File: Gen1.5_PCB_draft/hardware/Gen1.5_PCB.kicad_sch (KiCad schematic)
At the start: 45 parts, among them IC1 TJA1050T, J10 jumper2, J12 Enc2, J13 Enc3, J14 Enc4, J15 Enc5, J16 Enc6, J2 Booster, J3 Enc1, J4 jumper1, J5 Roboclaw1, J6 Roboclaw2, J7 Roboclaw3, U1 ESP32-P4-ETH, U2 4754, U8 level shifter

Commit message: fixed pcb
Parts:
- removed J10: jumper2, Gen1.5_PCB:CONN_3pin_jumper, symbol Connector_Generic:Conn_01x03
- removed J4: jumper1, Gen1.5_PCB:CONN_3pin_jumper, symbol Connector_Generic:Conn_01x03
- added S5: jumper1, Gen1.5_PCB:switch, symbol Gen1.5_PCB:switch
- added S6: jumper2, Gen1.5_PCB:switch, symbol Gen1.5_PCB:switch
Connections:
- net CANH: now also S5.3
- net CANL: now also S6.3
- net RX1: now also S5.1
- net TX1: now also S6.1
- net at J5.2 (Pin_2): now also S6.2
- net at J5.3 (Pin_3): now also S5.2

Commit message: added test points
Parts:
- added TP5, TP6, TP7: 5003, Gen1.5_PCB:test_point, symbol Gen1.5_PCB:5003
- J12: value Enc2 -> Enc3
- J13: value Enc3 -> Enc1
- J14: value Enc4 -> Enc6
- J15: value Enc5 -> Enc4
- J16: value Enc6 -> Enc2
- J3: value Enc1 -> Enc5
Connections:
- net 10V: now also TP7.TP
- net 3V3: now also TP5.TP
- net 5V: now also TP6.TP

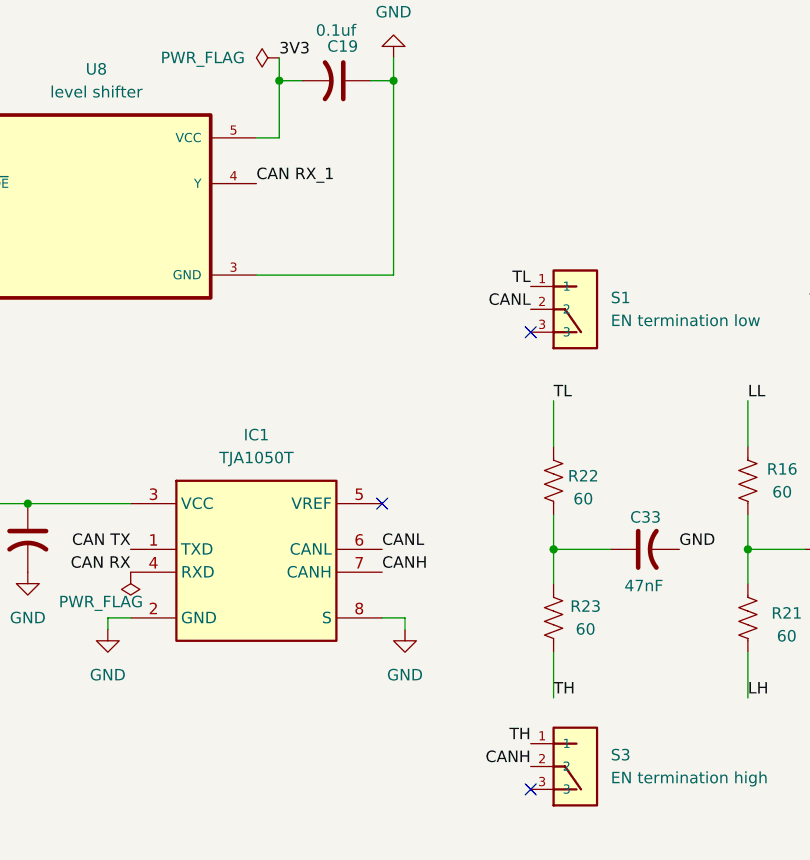
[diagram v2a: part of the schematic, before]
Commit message: added can test points
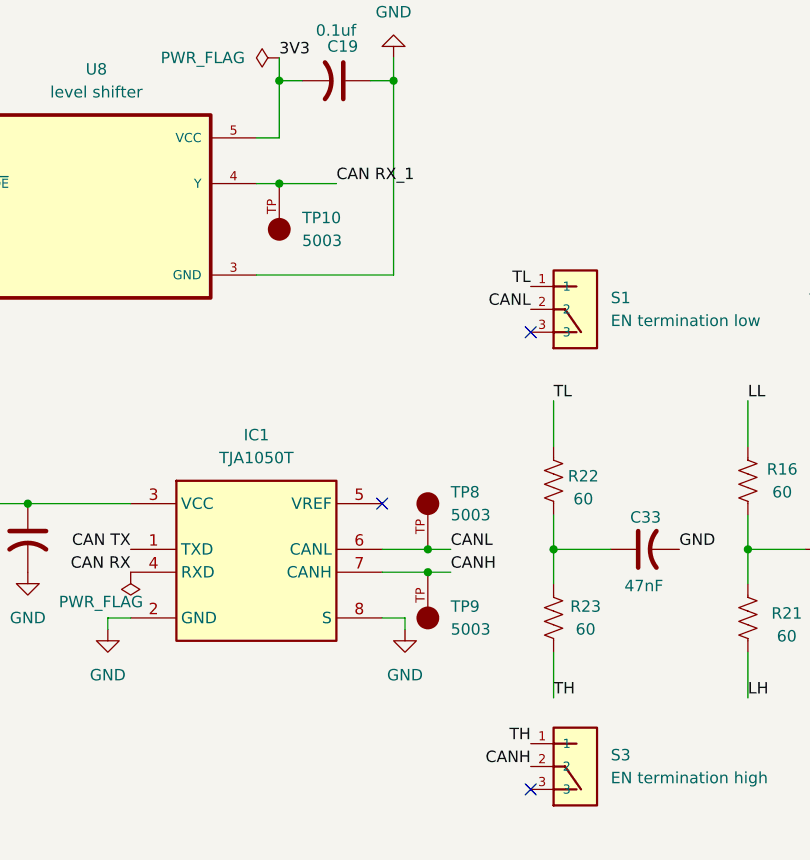
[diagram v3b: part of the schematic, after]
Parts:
- added TP10, TP8, TP9: 5003, Gen1.5_PCB:test_point, symbol Gen1.5_PCB:5003
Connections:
- net CAN RX_1: now also TP10.TP
- net CANH: now also TP9.TP
- net CANL: now also TP8.TP

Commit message: final changes before DR
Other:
- note added: "CAN"
- moved on the sheet: J2, TP7
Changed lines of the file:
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@@
 	)
 	(rectangle
-		(start 95.25 39.37)
-		(end 119.38 57.15)
+		(start 92.71 27.94)
+		(end 128.27 50.8)
 		(stroke
 			(width 0.381)
@@
 	(rectangle
 		(start 115.57 140.97)
-		(end 162.56 195.58)
+		(end 165.1 195.58)
 		(stroke
 			(width 0.381)
@@
 		)
 	)
+	(rectangle
+		(start 138.43 15.24)
+		(end 284.48 109.22)
+		(stroke
+			(width 0.381)
+			(type solid)
+			(color 0 255 0 1)
+		)
+		(fill
+			(type none)
+		)
+	)
 	(text "Boost conv"
 		(exclude_from_sim no)
-		(at 106.934 41.91 0)
+		(at 110.744 30.48 0)
 		(effects
 			(font
@@
 	(text ""
 		(exclude_from_sim no)
-		(at 96.52 54.356 0)
+		(at 100.33 42.926 0)
 		(effects
 			(font
@@
 		)
 	)
+	(text "CAN"
+		(exclude_from_sim no)
+		(at 225.044 19.558 0)
+		(effects
+			(font
+				(size 3.81 3.81)
+				(thickness 0.762)
+				(bold yes)
+				(color 0 255 0 1)
+			)
+		)
+	)
 	(text "load cells"
 		(exclude_from_sim no)
@@
 	(text ""
 		(exclude_from_sim no)
-		(at 120.65 55.626 0)
+		(at 124.46 44.196 0)
 		(effects
 			(font
@@
 	)
 	(junction
-		(at 102.87 53.34)
+		(at 106.68 41.91)
 		(diameter 0)
 		(color 0 0 0 0)
@@
 	)
 	(no_connect
-		(at 102.87 45.72)
+		(at 106.68 34.29)
 	)
 	(no_connect
@@
 	(wire
 		(pts
-			(xy 102.87 54.61) (xy 102.87 53.34)
+			(xy 106.68 43.18) (xy 106.68 41.91)
 		)
 		(stroke
@@
 	)
 	(label "GND"
-		(at 102.87 48.26 180)
+		(at 106.68 36.83 180)
 		(effects
 			(font
@@
 	)
 	(label "5V"
-		(at 102.87 50.8 180)
+		(at 106.68 39.37 180)
 		(effects
 			(font
@@
 	(global_label "10V"
 		(shape input)
-		(at 102.87 54.61 180)
+		(at 106.68 43.18 180)
 		(fields_autoplaced yes)
 		(effects
@@
 		)
 		(property "Intersheetrefs" "${INTERSHEET_REFS}"
-			(at 96.3772 54.61 0)
+			(at 100.1872 43.18 0)
 			(hide yes)
 			(show_name no)
@@
 	(symbol
 		(lib_id "Connector_Generic:Conn_01x04")
-		(at 107.95 48.26 0)
+		(at 111.76 36.83 0)
 		(unit 1)
 		(body_style 1)
@@
 		(fields_autoplaced yes)
 		(property "Reference" "J2"
-			(at 110.49 48.2599 0)
+			(at 114.3 36.8299 0)
 			(show_name no)
 			(do_not_autoplace no)
@@
 		)
 		(property "Value" "Booster"
-			(at 110.49 50.7999 0)
+			(at 114.3 39.3699 0)
 			(show_name no)
 			(do_not_autoplace no)
@@
 		)
 		(property "Footprint" "Gen1.5_PCB:booster headers"
-			(at 107.95 48.26 0)
+			(at 111.76 36.83 0)
 			(hide yes)
 			(show_name no)
@@
 		)
 		(property "Datasheet" ""
-			(at 107.95 48.26 0)
+			(at 111.76 36.83 0)
 			(hide yes)
 			(show_name no)
@@
 		)
 		(property "Description" "Generic connector, single row, 01x04, script generated (kicad-library-utils/schlib/autogen/connector/)"
-			(at 107.95 48.26 0)
+			(at 111.76 36.83 0)
 			(hide yes)
 			(show_name no)
@@
 		)
 		(property "LCSC" ""
-			(at 107.95 48.26 0)
+			(at 111.76 36.83 0)
 			(hide yes)
 			(show_name no)
@@
 	(symbol
 		(lib_id "Gen1.5_PCB:5003")
-		(at 102.87 58.42 270)
+		(at 106.68 46.99 270)
 		(unit 1)
 		(body_style 1)
@@
 		(fields_autoplaced yes)
 		(property "Reference" "TP7"
-			(at 105.41 57.1499 90)
+			(at 109.22 45.7199 90)
 			(show_name no)
 			(do_not_autoplace no)
@@
 		)
 		(property "Value" "5003"
-			(at 105.41 59.6899 90)
+			(at 109.22 48.2599 90)
 			(show_name no)
 			(do_not_autoplace no)
@@
 		)
 		(property "Footprint" "Gen1.5_PCB:test_point"
-			(at 102.87 58.42 0)
+			(at 106.68 46.99 0)
 			(hide yes)
 			(show_name no)
@@
 		)
 		(property "Datasheet" ""
-			(at 102.87 58.42 0)
+			(at 106.68 46.99 0)
 			(hide yes)
 			(show_name no)
@@
 		)
 		(property "Description" ""
-			(at 102.87 58.42 0)
+			(at 106.68 46.99 0)
 			(hide yes)
 			(show_name no)
@@
 		)
 		(property "PARTREV" "H"
-			(at 102.87 58.42 0)
+			(at 106.68 46.99 0)
 			(hide yes)
 			(show_name no)
@@
 		)
 		(property "STANDARD" "Manufacturer Recommendations"
-			(at 102.87 58.42 0)
+			(at 106.68 46.99 0)
 			(hide yes)
 			(show_name no)
@@
 		)
 		(property "SNAPEDA_PN" "5000"
-			(at 102.87 58.42 0)
+			(at 106.68 46.99 0)
 			(hide yes)
 			(show_name no)
@@
 		)
 		(property "MAXIMUM_PACKAGE_HEIGHT" "4.57 mm"
-			(at 102.87 58.42 0)
+			(at 106.68 46.99 0)
 			(hide yes)
 			(show_name no)
@@
 		)
 		(property "MANUFACTURER" "Keystone"
-			(at 102.87 58.42 0)
+			(at 106.68 46.99 0)
 			(hide yes)
 			(show_name no)
@@
 		)
 		(property "LCSC" "C238124"
-			(at 102.87 58.42 90)
+			(at 106.68 46.99 90)
 			(hide yes)
 			(show_name no)
@@
 	(symbol
 		(lib_id "power:PWR_FLAG")
-		(at 102.87 50.8 90)
+		(at 106.68 39.37 90)
 		(unit 1)
 		(body_style 1)
@@
 		(fields_autoplaced yes)
 		(property "Reference" "#FLG02"
-			(at 100.965 50.8 0)
+			(at 104.775 39.37 0)
 			(hide yes)
 			(show_name no)
@@
 		)
 		(property "Value" "PWR_FLAG"
-			(at 99.06 50.7999 90)
+			(at 102.87 39.3699 90)
 			(show_name no)
 			(do_not_autoplace no)
@@
 		)
 		(property "Footprint" ""
-			(at 102.87 50.8 0)
+			(at 106.68 39.37 0)
 			(hide yes)
 			(show_name no)
@@
 		)
 		(property "Datasheet" ""
-			(at 102.87 50.8 0)
+			(at 106.68 39.37 0)
 			(hide yes)
 			(show_name no)
@@
 		)
 		(property "Description" "Special symbol for telling ERC where power comes from"
-			(at 102.87 50.8 0)
+			(at 106.68 39.37 0)
 			(hide yes)
 			(show_name no)

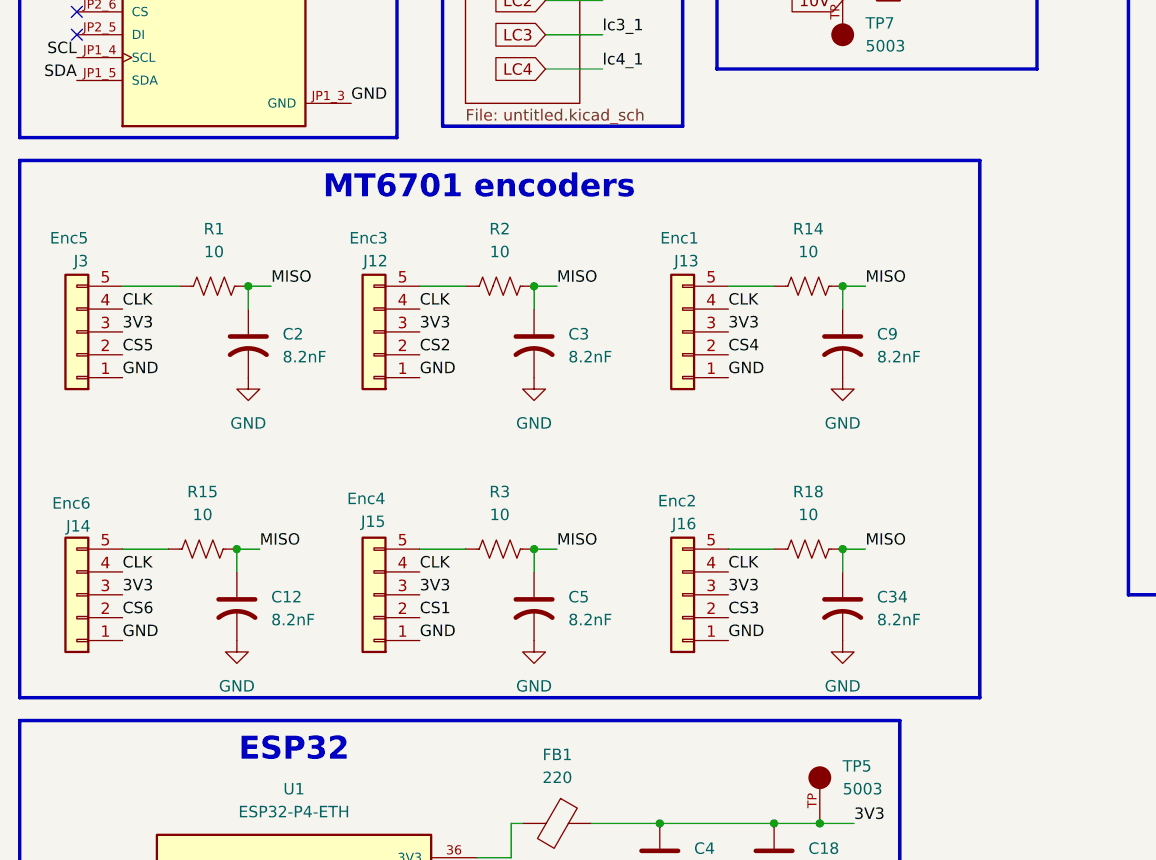
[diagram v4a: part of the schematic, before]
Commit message: finished mcp connector design
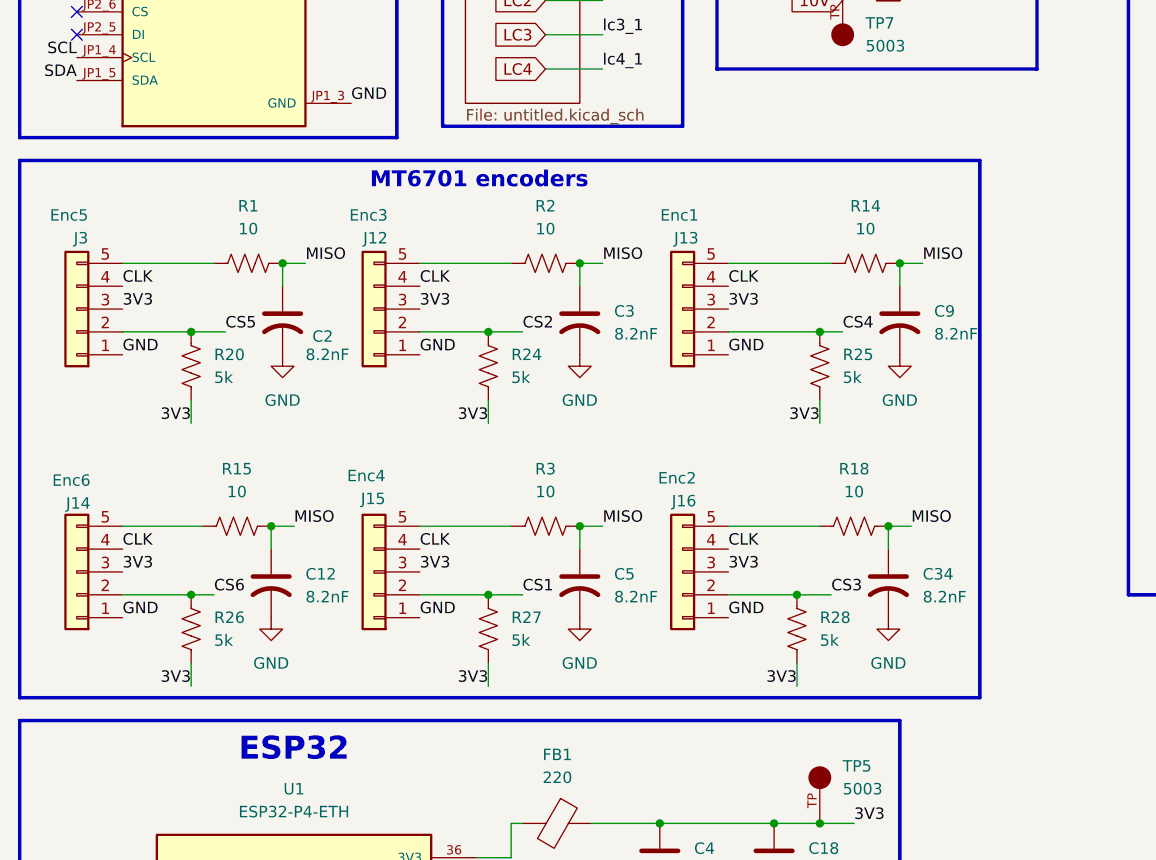
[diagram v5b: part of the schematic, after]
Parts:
- added R20, R24, R25, R26, R27, R28: 5k, Gen1.5_PCB:RES_5k, symbol Device:R_US
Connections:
- net 3V3: now also R20.1, R24.1, R25.1, R26.1, R27.1, R28.1
- net CS1: now also R27.2
- net CS2: now also R24.2
- net CS3: now also R28.2
- net CS4: now also R25.2
- net CS5: now also R20.2
- net CS6: now also R26.2
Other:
- moved on the sheet: C12, C2, C3, C34, C5, C9, J12, J13, J14, J15, J16, J3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
